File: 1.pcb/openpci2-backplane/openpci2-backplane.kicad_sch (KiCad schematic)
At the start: 14 parts

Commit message: Reduced number of x1 and M.2 connectors, resized PCB
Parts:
- LOGO4: Label (none) -> Raspberry Pi
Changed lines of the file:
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@@
+			)
+		)
+		(property "DigiKey" ""
+			(at 116.84 170.18 0)
+			(effects
+				(font
+					(size 1.27 1.27)
+				)
+				(hide yes)
+			)
+		)
+		(property "Mouser" ""
+			(at 116.84 170.18 0)
+			(effects
+				(font
+					(size 1.27 1.27)
+				)
+				(hide yes)
+			)
+		)
+		(property "TME" ""
+			(at 116.84 170.18 0)
+			(effects
+				(font
+					(size 1.27 1.27)
+				)
+				(hide yes)
+			)
+		)
+		(property "LCSC" ""
+			(at 116.84 170.18 0)
+			(effects
+				(font
+					(size 1.27 1.27)
+				)
+				(hide yes)
+			)
+		)
+		(property "Label" "Raspberry Pi"
+			(at 116.84 170.18 0)
+			(effects
+				(font
+					(size 0.889 0.889)
+				)
+				(hide yes)
 			)
 		)

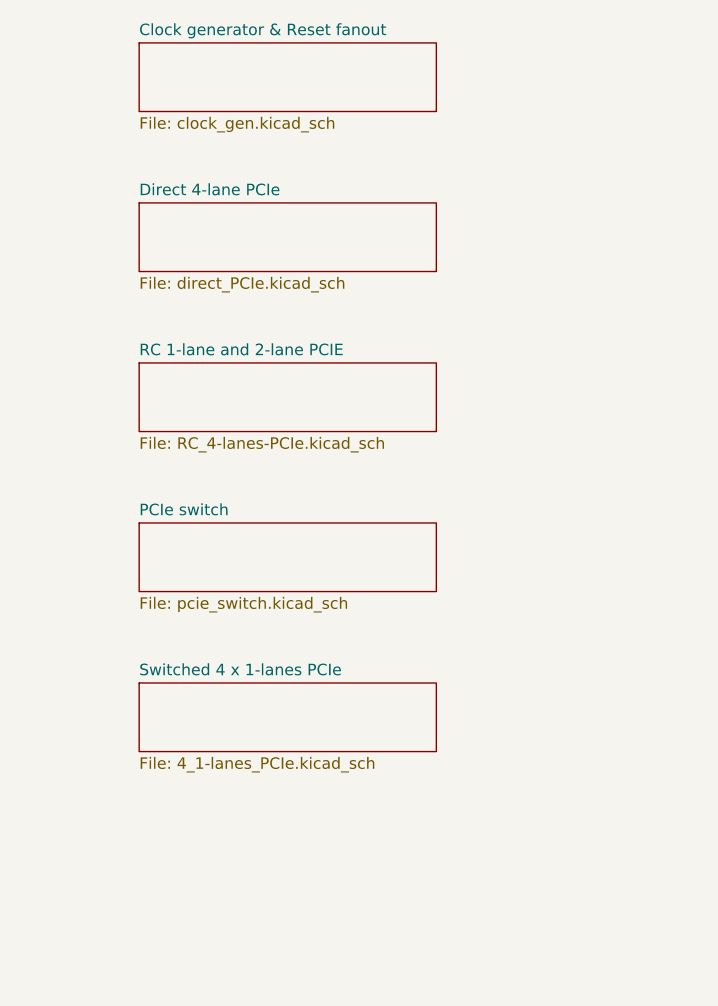
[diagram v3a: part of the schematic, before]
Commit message: Schematic: Cleanup and revision
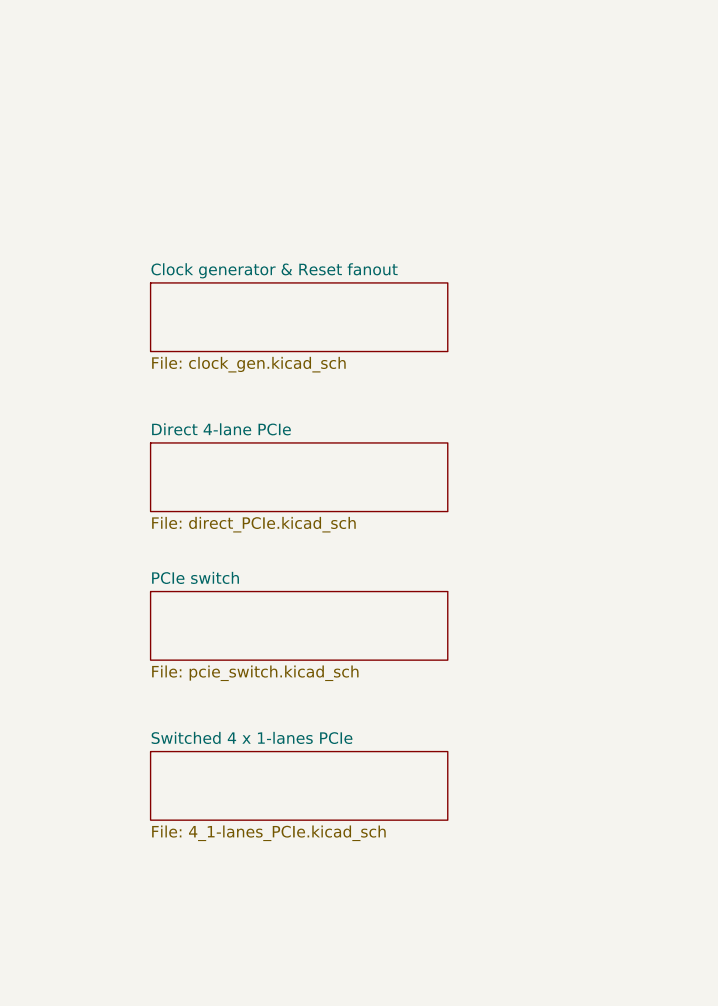
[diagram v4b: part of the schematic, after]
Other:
- removed sheet RC 1-lane and 2-lane PCIE

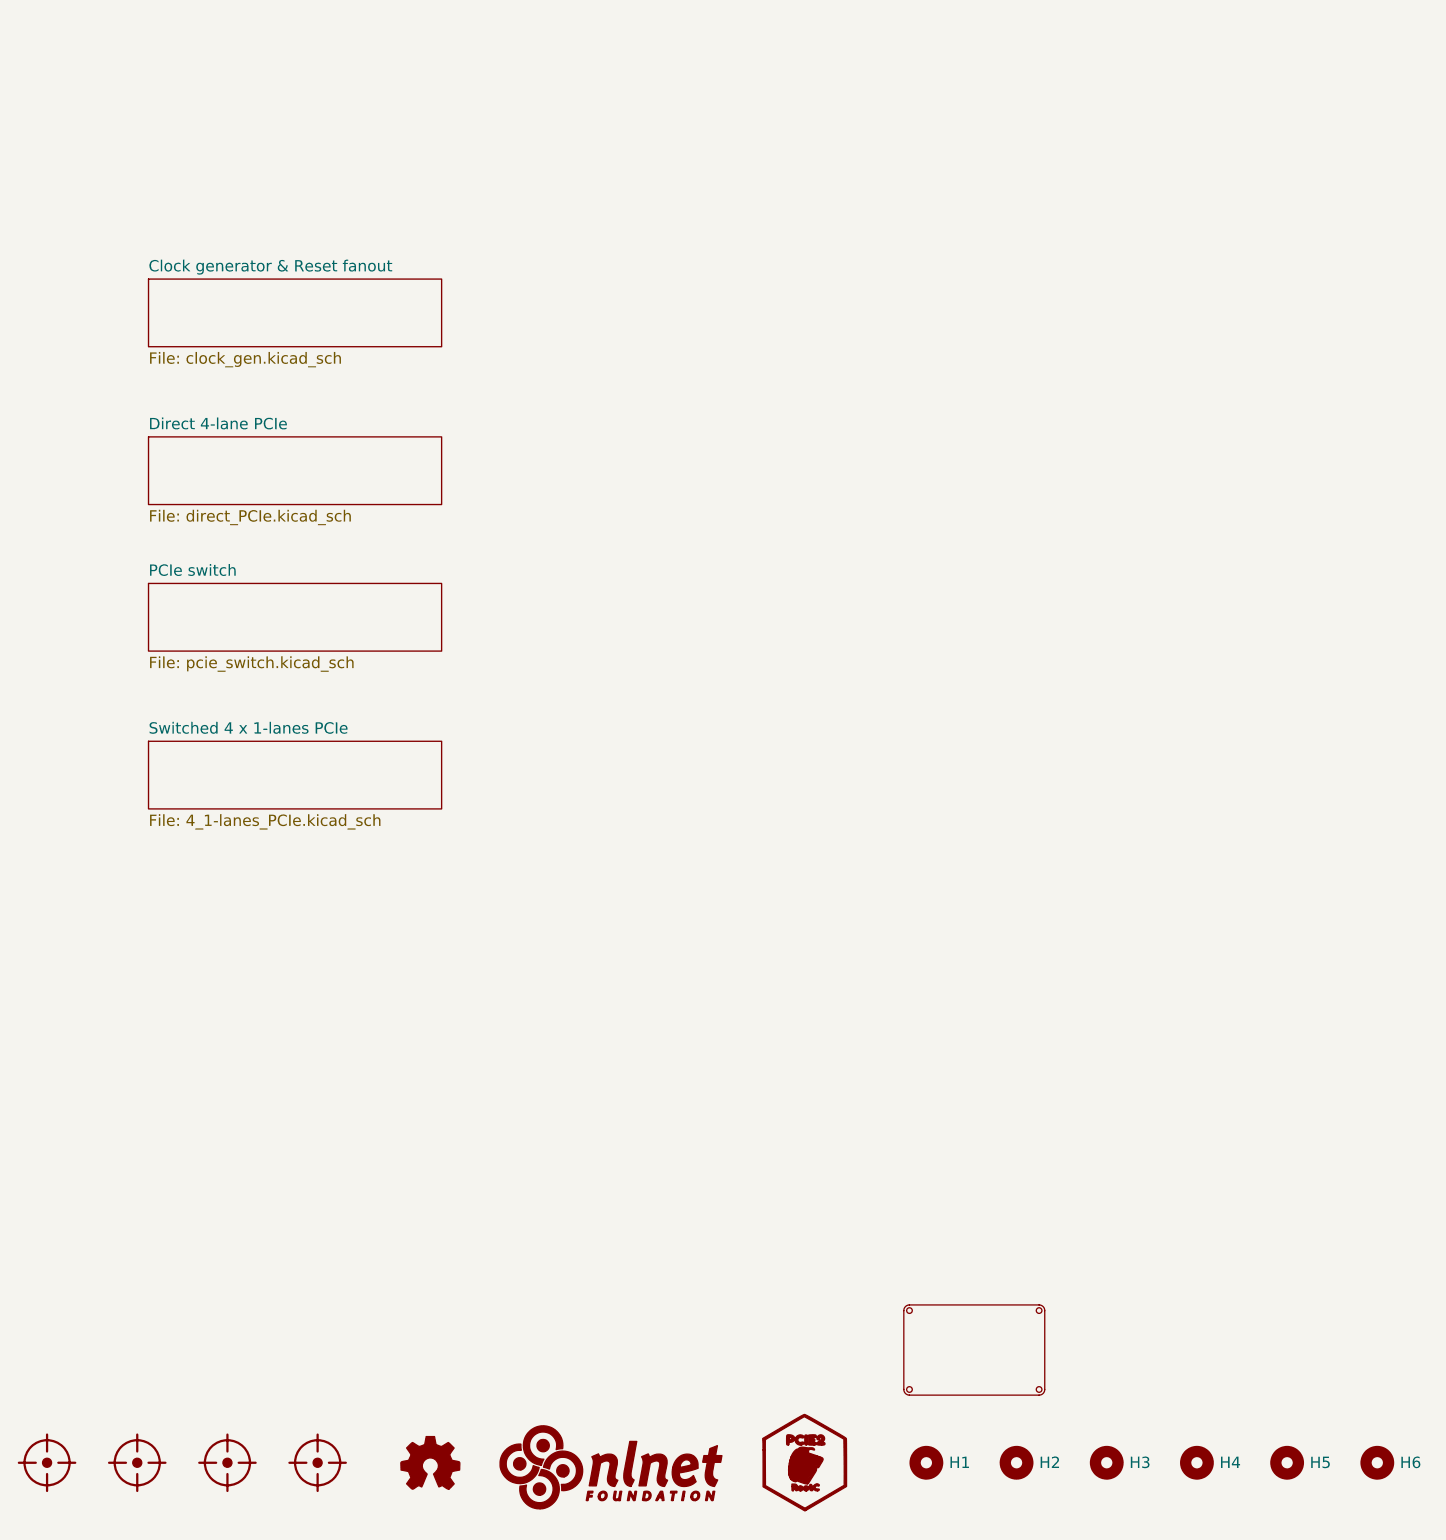
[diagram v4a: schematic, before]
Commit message: Schematic: Cleanup, revision and layout improvements
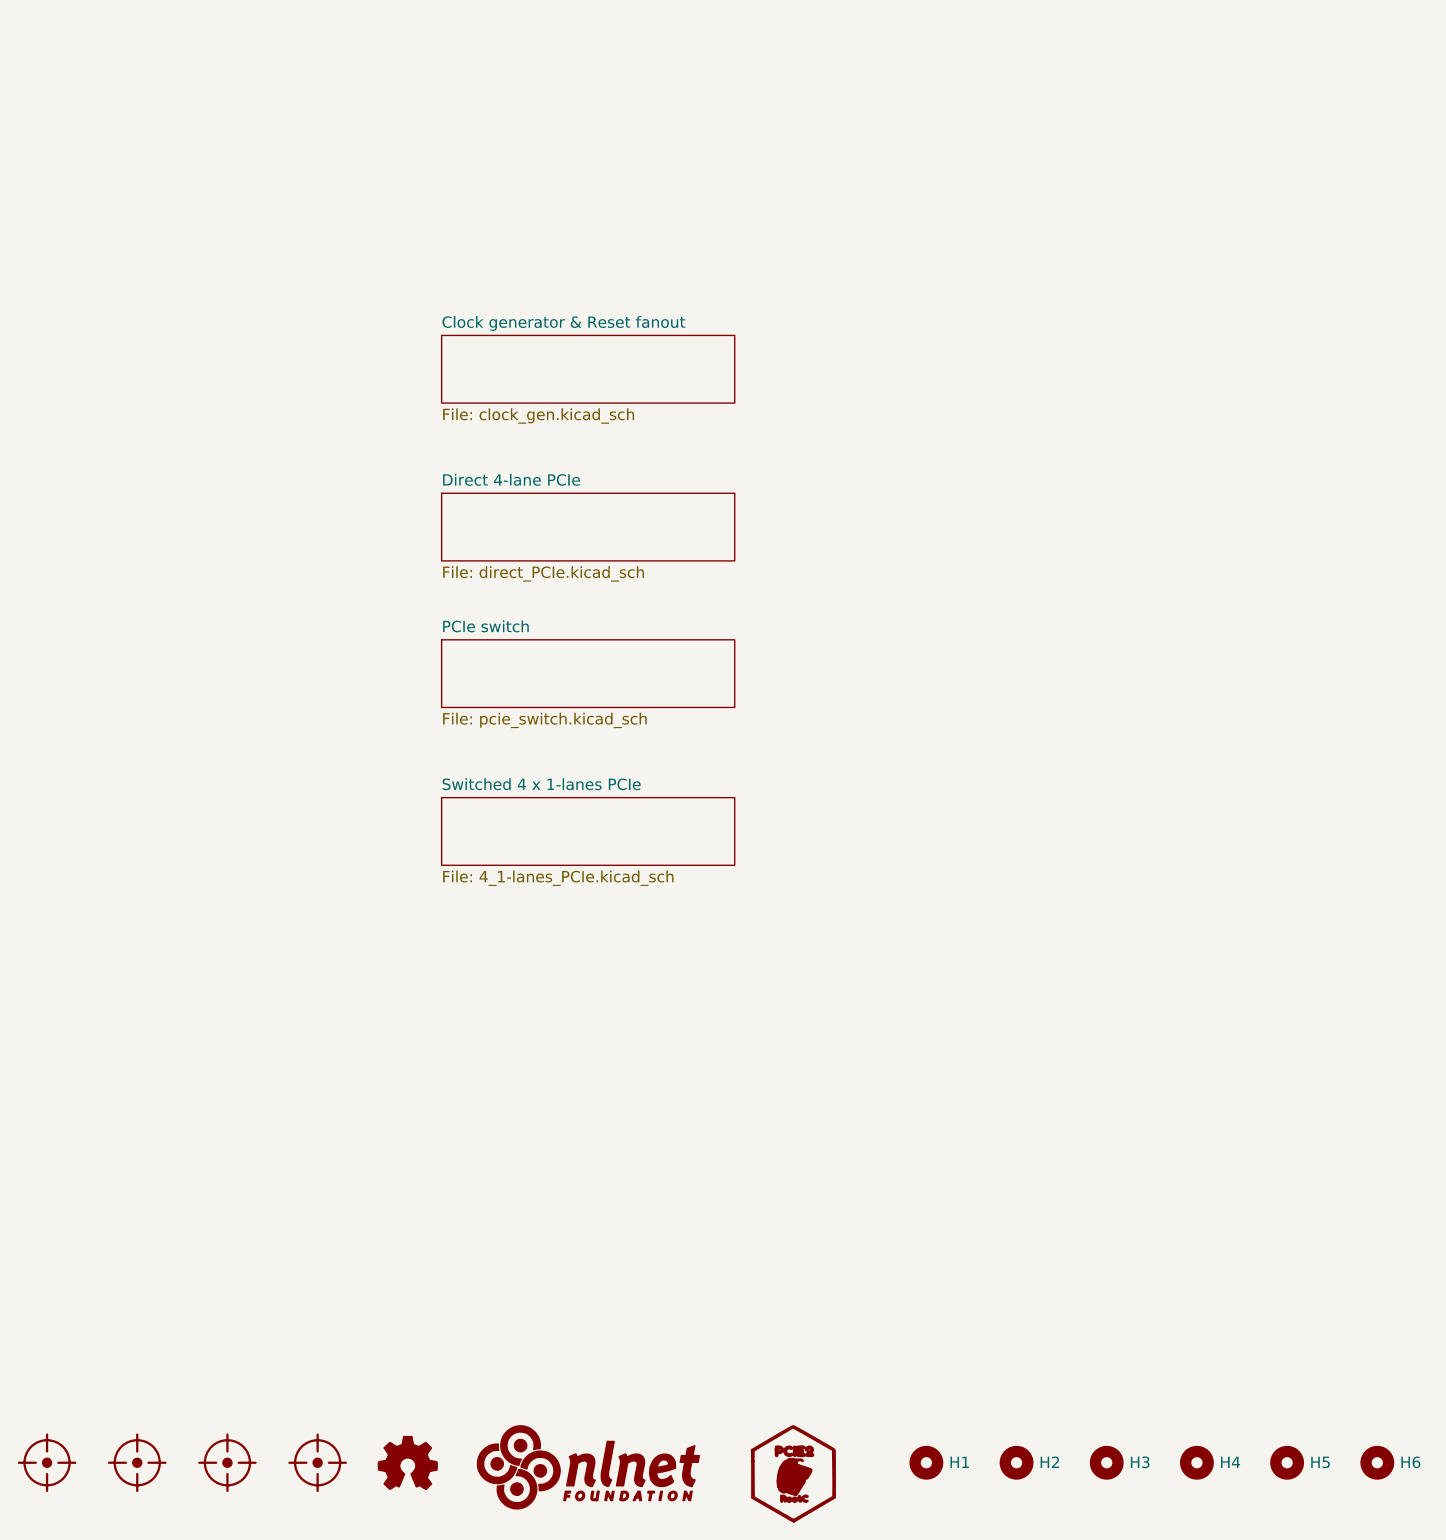
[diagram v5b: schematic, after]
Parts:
- removed LOGO4: ~, PCM_Chili-chips:Raspberry-Pi-4 outline, symbol PCM_Chili-chips:Raspberry Pi outline

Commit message: Schematic: Cleanup, revision and layout improvements
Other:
- company: Chili.CHIPS -> Chili.CHIPS*ba

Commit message: Final PCB layout revision, ready for manufacturing
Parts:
- LOGO3: footprint PCM_Chili-chips:PCIE2 logo -> PCM_av_lib:PCIE2 logo
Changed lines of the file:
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@@
 			)
 		)
-		(property "Footprint" "PCM_Chili-chips:PCIE2 logo"
+		(property "Footprint" "PCM_av_lib:PCIE2 logo"
 			(at 102.87 199.5884 0)
 			(effects
